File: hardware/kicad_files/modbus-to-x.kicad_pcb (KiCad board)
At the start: 4 copper layers, 87.6 x 46.7 mm, 67 parts, among them IC1 ESP32-WROOM-32D_M113DH2800PH3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, J1 615006138421, J4 M50-3140545R, Q1 DSS4160U-7, Q2 DSS4160U-7, SW1 SW_Wuerth_450301014042, SW4 3983, U1 LM2596S-3.3, U3 MAX3485, Y1 32.768kHz

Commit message: redo
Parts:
- removed ? (x27): , 
- moved C6 15.0 mm to (51.9, 100.3)
- moved C8 2.97 mm to (76.6, 102.9)
- moved C1 2.24 mm to (71.6, 102.9)
- moved L1 0.35 mm to (66.6, 116.8)
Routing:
- net GND: track 36.1 -> 88.3 mm, vias 321 -> 320
- net VDD33: vias 35 -> 28

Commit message: wip
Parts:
- moved SW4 9.44 mm to (98.8, 110.1), turned to 90 degrees
- moved C2 3.08 mm to (94.2, 109.3), turned to -90 degrees
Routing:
- net GND: track 88.3 -> 91.7 mm, vias 320 -> 317
- net /EN: track 42.1 -> 39.0 mm
- net VDD33: vias 28 -> 20

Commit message: wip
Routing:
- net GND: track 91.7 -> 246.5 mm, vias 317 -> 322

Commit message: wip
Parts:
- removed D3: SMAJ12A, Diode_SMD:D_SMA_Handsoldering
- removed R20: 10K, Resistor_SMD:R_0805_2012Metric_Pad1.20x1.40mm_HandSolder
- removed Y1: 32.768kHz, project_footprints:XTAL_ABS05-32.768KHZ-T
- added D7: SS56, Diode_SMD:D_SMA, F.Cu at (77.0, 136.8)
- added D8: SMAJ12A, Diode_SMD:D_SMA, F.Cu at (77.0, 141.3)
- added F1: 2920L150, Fuse:Fuse_2920_7451Metric, F.Cu at (78.1, 131.0)
- added R5: 10K, Resistor_SMD:R_0603_1608Metric, F.Cu at (106.7, 108.2)
- C2, C24: footprint Capacitor_SMD:C_1206_3216Metric_Pad1.33x1.80mm_HandSolder -> Capacitor_SMD:C_0805_2012Metric
- C3: value 12pF -> 0.1uF; footprint Capacitor_SMD:C_0402_1005Metric_Pad0.74x0.62mm_HandSolder -> Capacitor_SMD:C_0805_2012Metric
- C5: value 12pF -> 4.7uF; footprint Capacitor_SMD:C_0402_1005Metric_Pad0.74x0.62mm_HandSolder -> Capacitor_SMD:C_0805_2012Metric
- R19, R4: footprint Resistor_SMD:R_0805_2012Metric_Pad1.20x1.40mm_HandSolder -> Resistor_SMD:R_0603_1608Metric
- moved C5 51.3 mm to (54.8, 109.1)
- moved C3 50.8 mm to (54.8, 107.1)
- moved D1 18.3 mm to (90.8, 117.0), turned to 180 degrees
- moved R3 12.4 mm to (91.3, 114.4), turned to 180 degrees
- moved L1 8.63 mm to (74.0, 112.5)
- moved C1 4.95 mm to (76.5, 101.9)
- moved C8 4.95 mm to (81.5, 101.9)
- moved U1 4.85 mm to (68.2, 95.8)
- moved D2 4.45 mm to (62.8, 107.8)
- moved C6 2.75 mm to (54.4, 101.5), turned to 0 degrees
- moved SW1 2.31 mm to (90.8, 123.9), turned to -90 degrees
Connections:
- C3 pad 1: GND -> /V_BUCK
- C3 pad 2: /X32N -> GND
- C5 pad 1: GND -> /V_BUCK
- C5 pad 2: /X32P -> GND
- J1 pad 6: /V_IN -> /V_EXT
- SW1 pad 1: /V_IN -> /V_PROT
- SW1 pad 2: /V_IN -> /V_PROT
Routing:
- net GND: track 246.5 -> 54.6 mm, vias 322 -> 203
- net VDD33: track 16.3 -> 37.6 mm, vias 20 -> 18
- net /V_BUCK: track 0.27 -> 5.90 mm
- net Net-(D2-A1): track 5.61 -> 10.1 mm
- net /X32P: track 3.29 -> 0.00 mm
- net /X32N: track 3.17 -> 0.00 mm
- added copper zone on F.Cu, net /V_PROT
- removed copper zone on F.Cu, net /V_IN
- removed copper zone on F.Cu, net Net-(D2-A1)
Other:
- outline, holes or cut-outs redrawn
- board text removed: "1"

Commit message: wip
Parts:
- moved SW1 24.0 mm to (66.9, 125.6)
- moved D8 18.4 mm to (87.2, 126.0), turned to 90 degrees
- moved F1 17.4 mm to (94.7, 125.9)
- moved D7 13.1 mm to (89.0, 131.5)
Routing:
- net GND: vias 203 -> 198
- added copper zone on F.Cu, net /V_EXT
- removed copper zone on F.Cu, net /V_PROT
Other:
- board text removed: "V_SW"

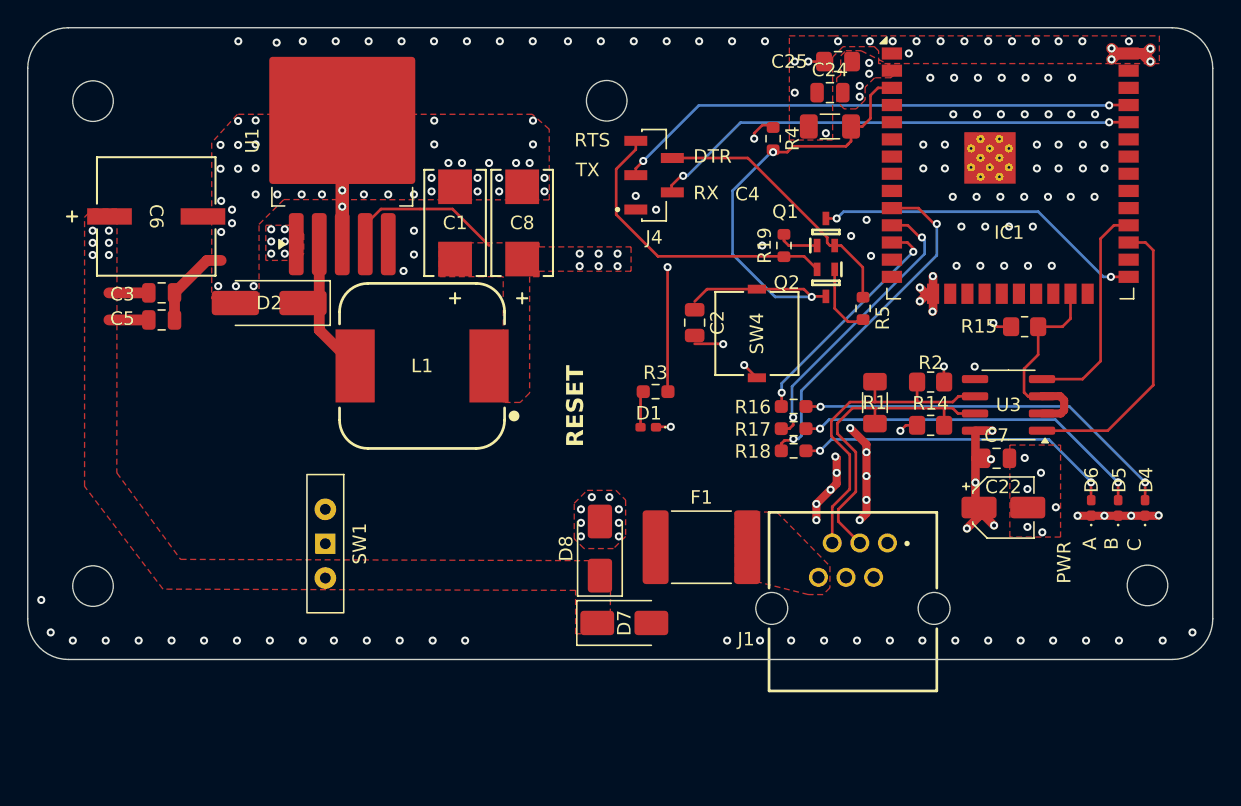
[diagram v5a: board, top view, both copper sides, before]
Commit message: small trace refinements
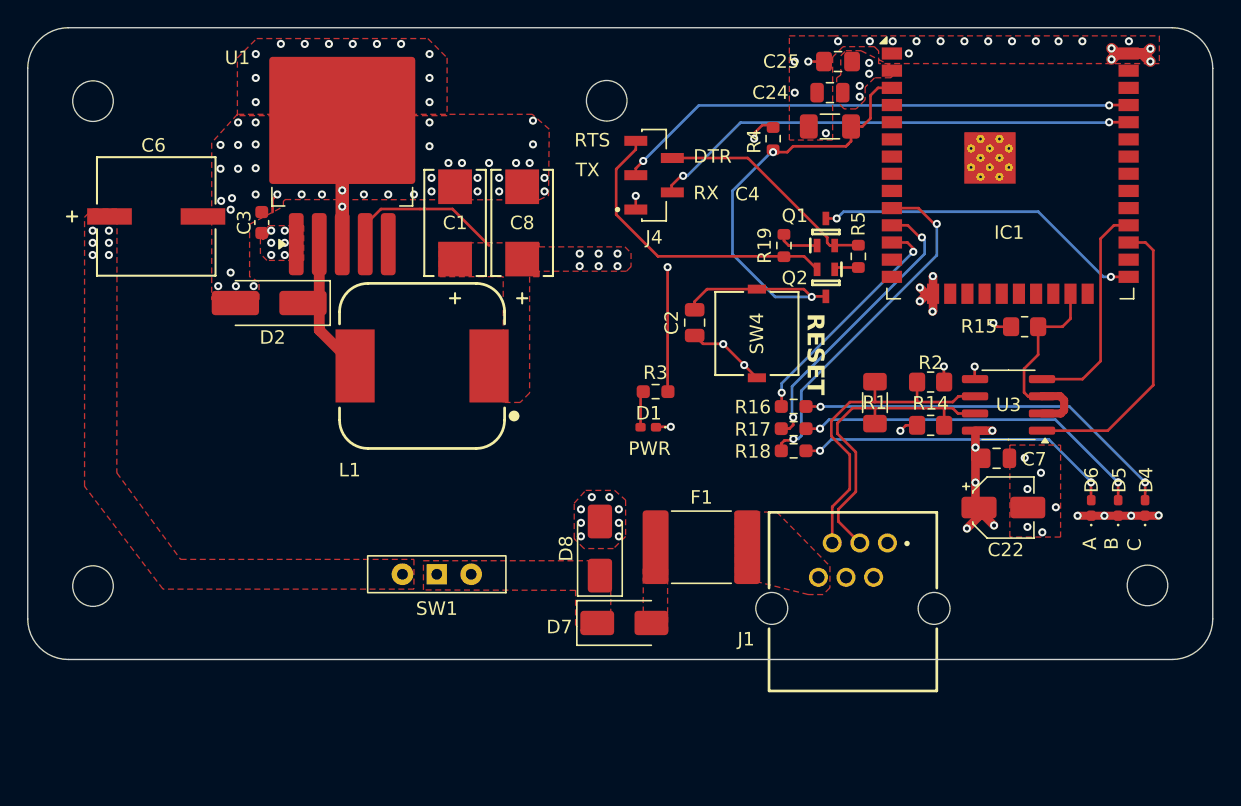
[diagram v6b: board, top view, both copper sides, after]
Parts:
- removed C5: 4.7uF, Capacitor_SMD:C_0805_2012Metric
- C3: footprint Capacitor_SMD:C_0805_2012Metric -> Capacitor_SMD:C_0603_1608Metric
- moved C3 9.04 mm to (62.2, 101.9), turned to 90 degrees
- moved SW1 8.54 mm to (75.1, 127.9), turned to 180 degrees
- moved R5 3.87 mm to (106.3, 104.4)
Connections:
- IC1 pad 8: /X32P -> unconnected-(IC1-IO32-Pad8)
- IC1 pad 9: /X32N -> unconnected-(IC1-IO33-Pad9)
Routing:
- net GND: track 54.6 -> 41.1 mm, vias 198 -> 103
- net /V_BUCK: track 5.90 -> 0.87 mm
- net Net-(Q2-B): track 5.38 -> 1.80 mm
- net /DTR: track 19.7 -> 16.7 mm
- net /EN: track 39.0 -> 39.6 mm
- added copper zone on F.Cu, net /V_PROT
- added copper zone on F.Cu, net Net-(D7-A)
